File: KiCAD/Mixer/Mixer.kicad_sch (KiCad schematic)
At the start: 20 parts, among them J1 IN_1, J2 IN_2, J3 OUT, J5 Conn_01x03_Socket, J6 Conn_01x03_Socket, Q1 ??, U1 TL072

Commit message: Mixer Schematic
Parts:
- R1, R2, R3, R4, R8: value R -> 100k
- R5: value R -> 1M
- R6: value R -> 220R
- R7: value R -> ??R
- RV1, RV2: value R_Pot -> 100k
- RV3: value NOISE -> 100k NOISE
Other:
- note added: "MYSTERY VERTICAL RESISTOR"
- moved on the sheet: J5, J6

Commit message: Mixer Footprint Association
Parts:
- C1, C2: footprint (none) -> HackSynth:C_Disc_D5.0mm_W2.5mm_P5.00mm
- J1, J2, J3: footprint (none) -> HackSynth:Jack_3.5mm
- R1, R2, R3, R4, R5, R6, R7, R8: footprint (none) -> HackSynth:R_Axial_DIN0207_L6.3mm_D2.5mm_P7.62mm_Horizontal
- RV1, RV2, RV3: footprint (none) -> HackSynth:Potentiometer_Alps_RK09K_Horizontal
- U1: footprint (none) -> HackSynth:DIP-8_W7.62mm_LongPads
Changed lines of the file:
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@@
 			)
 		)
-		(property "Footprint" ""
+		(property "Footprint" "HackSynth:Potentiometer_Alps_RK09K_Horizontal"
 			(at 64.77 104.14 0)
 			(effects
@@
 			)
 		)
-		(property "Footprint" ""
+		(property "Footprint" "HackSynth:Jack_3.5mm"
 			(at 82.55 87.63 0)
 			(effects
@@
 			)
 		)
-		(property "Footprint" ""
+		(property "Footprint" "HackSynth:DIP-8_W7.62mm_LongPads"
 			(at 161.29 118.11 0)
 			(effects
@@
 			)
 		)
-		(property "Footprint" ""
+		(property "Footprint" "HackSynth:R_Axial_DIN0207_L6.3mm_D2.5mm_P7.62mm_Horizontal"
 			(at 123.19 89.408 90)
 			(effects
@@
 			)
 		)
-		(property "Footprint" ""
+		(property "Footprint" "HackSynth:R_Axial_DIN0207_L6.3mm_D2.5mm_P7.62mm_Horizontal"
 			(at 125.222 114.3 90)
 			(effects
@@
 			)
 		)
-		(property "Footprint" ""
+		(property "Footprint" "HackSynth:Potentiometer_Alps_RK09K_Horizontal"
 			(at 127 104.14 0)
 			(effects
@@
 			)
 		)
-		(property "Footprint" ""
+		(property "Footprint" "HackSynth:R_Axial_DIN0207_L6.3mm_D2.5mm_P7.62mm_Horizontal"
 			(at 62.992 114.3 90)
 			(effects
@@
 			)
 		)
-		(property "Footprint" ""
+		(property "Footprint" "HackSynth:R_Axial_DIN0207_L6.3mm_D2.5mm_P7.62mm_Horizontal"
 			(at 146.812 128.27 90)
 			(effects
@@
 			)
 		)
-		(property "Footprint" ""
+		(property "Footprint" "HackSynth:C_Disc_D5.0mm_W2.5mm_P5.00mm"
 			(at 187.6552 121.92 0)
 			(effects
@@
 			)
 		)
-		(property "Footprint" ""
+		(property "Footprint" "HackSynth:Jack_3.5mm"
 			(at 168.91 88.9 0)
 			(effects
@@
 			)
 		)
-		(property "Footprint" ""
+		(property "Footprint" "HackSynth:DIP-8_W7.62mm_LongPads"
 			(at 123.19 66.04 0)
 			(effects
@@
 			)
 		)
-		(property "Footprint" ""
+		(property "Footprint" "HackSynth:R_Axial_DIN0207_L6.3mm_D2.5mm_P7.62mm_Horizontal"
 			(at 87.122 114.3 90)
 			(effects
@@
 			)
 		)
-		(property "Footprint" ""
+		(property "Footprint" "HackSynth:DIP-8_W7.62mm_LongPads"
 			(at 161.29 118.11 0)
 			(effects
@@
 			)
 		)
-		(property "Footprint" ""
+		(property "Footprint" "HackSynth:R_Axial_DIN0207_L6.3mm_D2.5mm_P7.62mm_Horizontal"
 			(at 131.572 43.18 90)
 			(effects
@@
 			)
 		)
-		(property "Footprint" ""
+		(property "Footprint" "HackSynth:R_Axial_DIN0207_L6.3mm_D2.5mm_P7.62mm_Horizontal"
 			(at 105.918 78.74 90)
 			(effects
@@
 			)
 		)
-		(property "Footprint" ""
+		(property "Footprint" "HackSynth:Potentiometer_Alps_RK09K_Horizontal"
 			(at 88.9 104.14 0)
 			(effects
@@
 			)
 		)
-		(property "Footprint" ""
+		(property "Footprint" "HackSynth:C_Disc_D5.0mm_W2.5mm_P5.00mm"
 			(at 119.38 49.8348 0)
 			(effects
@@
 			)
 		)
-		(property "Footprint" ""
+		(property "Footprint" "HackSynth:Jack_3.5mm"
 			(at 58.42 87.63 0)
 			(effects
@@
 			)
 		)
-		(property "Footprint" ""
+		(property "Footprint" "HackSynth:R_Axial_DIN0207_L6.3mm_D2.5mm_P7.62mm_Horizontal"
 			(at 114.808 78.74 90)
 			(effects

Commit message: Mixer Schematic
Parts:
- removed Q1: ??, Package_TO_SOT_THT:TO-92_Inline, symbol Transistor_BJT:2N3905
- added Q2: 2N3904 ?, Package_TO_SOT_THT:TO-92_Inline, symbol Transistor_BJT:2N3904
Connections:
- net GND: now also Q2.2 (B)
- net at C2.2, R8.1: now also Q2.1 (E)
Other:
- note added: "BC547 Fits?"
- note added: "I found a couple of examples of a 2N3904 used as a noise source with pin 3 disconnected. The schematic arrangement doesn't match the photo."
- note added: "https://www.eddybergman.com/2020/05/synthesizer-build-part-31-noise-module.html"
- moved on the sheet: J6

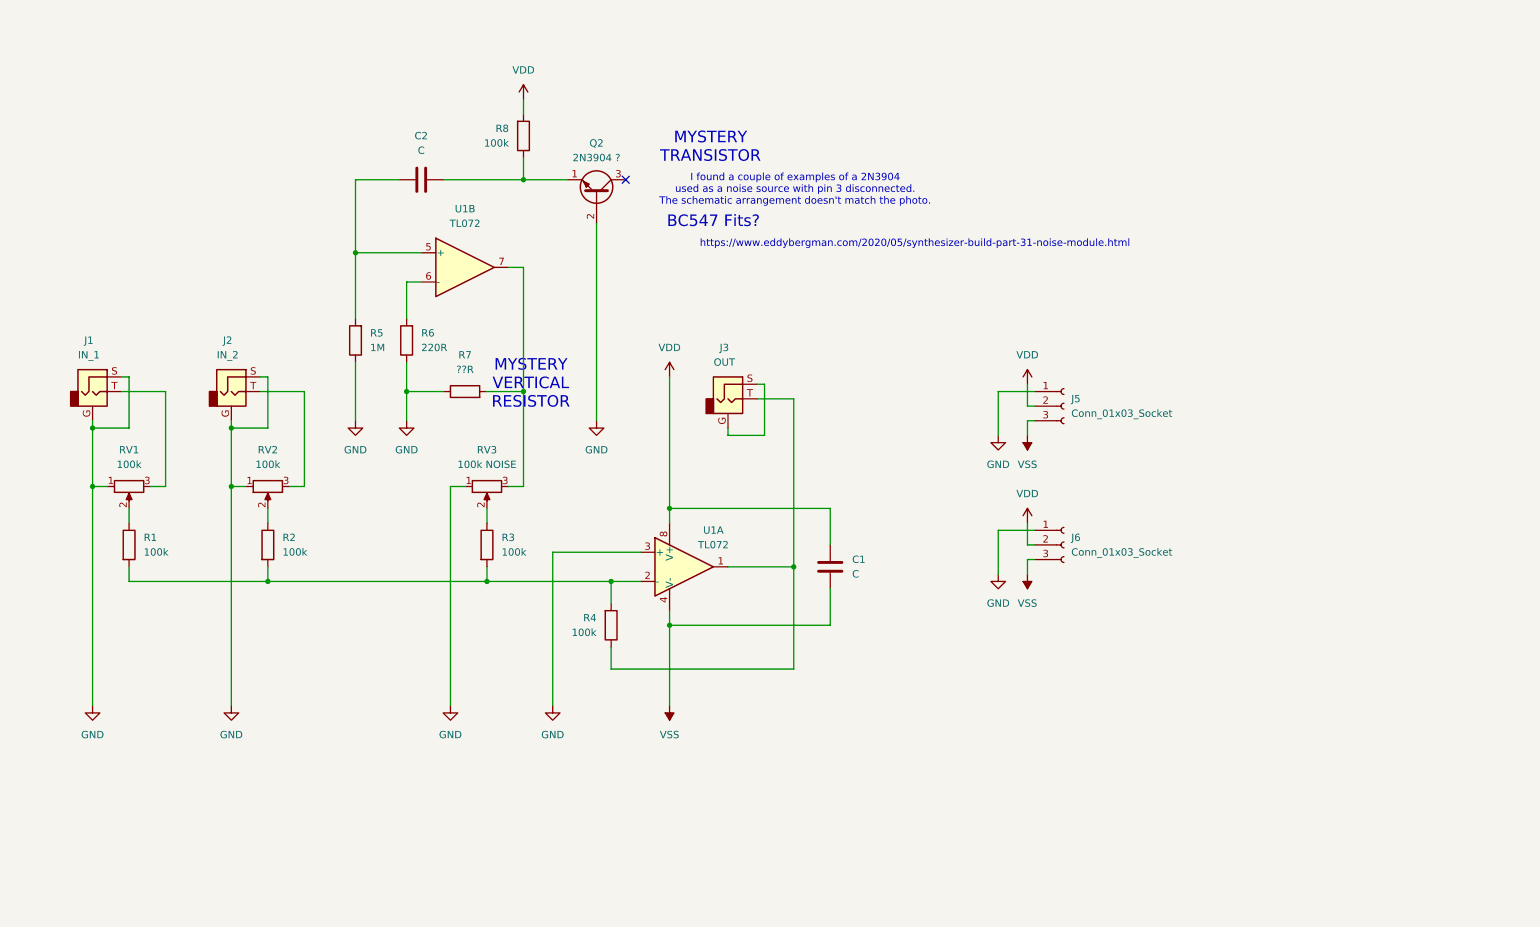
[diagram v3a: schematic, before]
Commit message: Mixer PCB
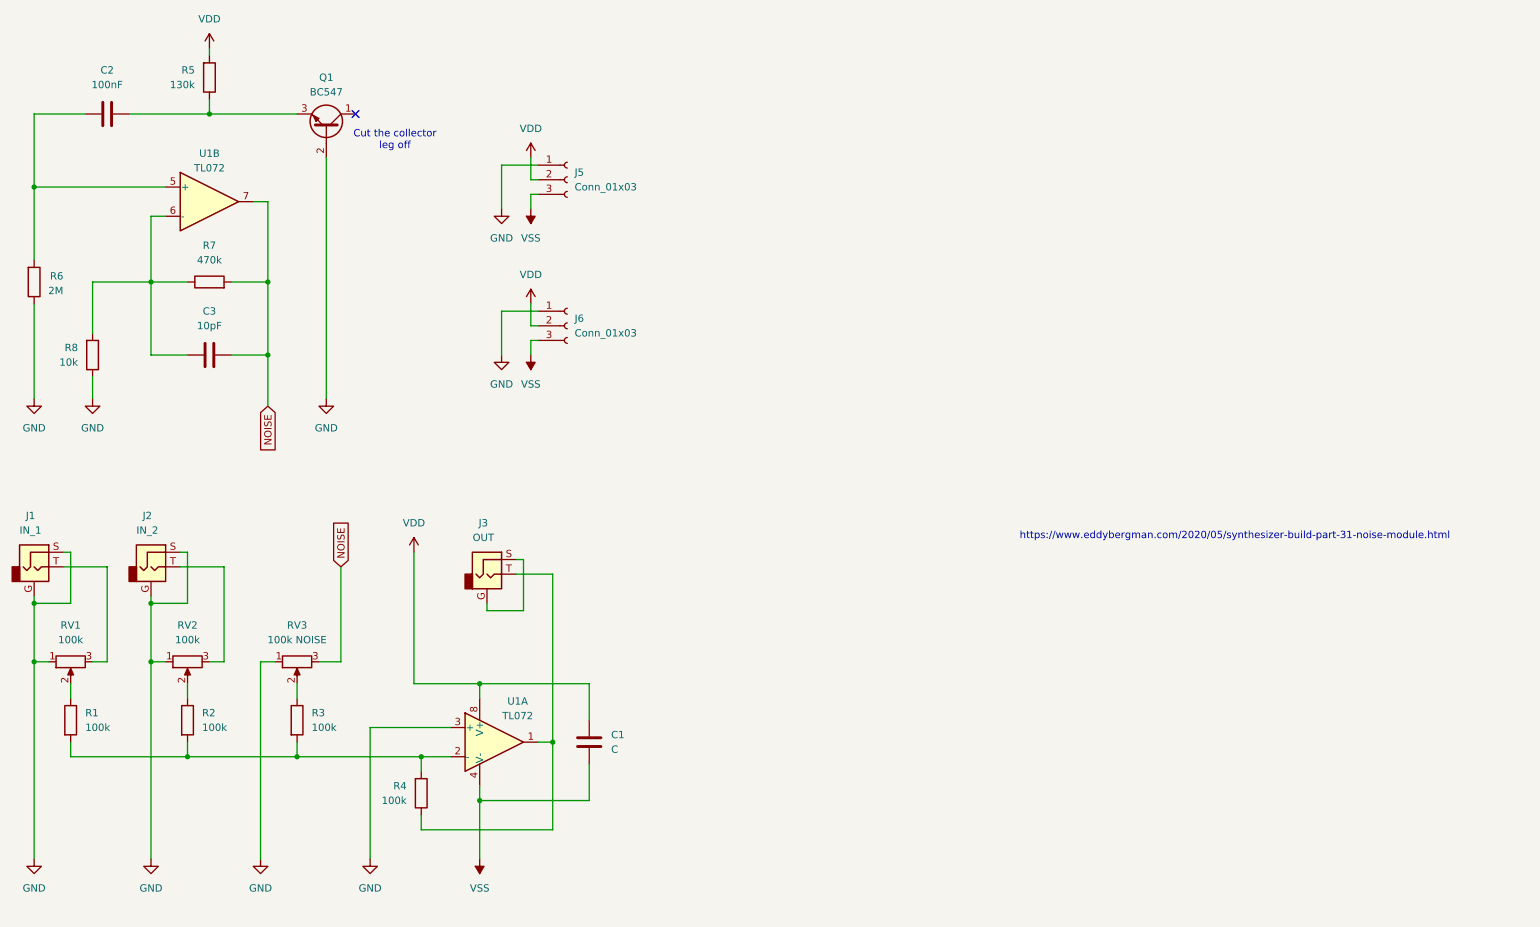
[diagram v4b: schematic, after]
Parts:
- removed Q2: 2N3904 ?, Package_TO_SOT_THT:TO-92_Inline, symbol Transistor_BJT:2N3904
- added C3: 10pF, HackSynth:C_Disc_D5.0mm_W2.5mm_P5.00mm, symbol Device:C
- added Q1: BC547, HackSynth:TO-92_Inline - BC547 - 2-Pin Handsolder, symbol Transistor_BJT:BC547
- C2: value C -> 100nF
- J5, J6: value Conn_01x03_Socket -> Conn_01x03
- R5: value 1M -> 130k
- R6: value 220R -> 2M
- R7: value ??R -> 470k
- R8: value 100k -> 10k
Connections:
- net GND: now also R8.1, Q1.2 (B); no longer R5.1, R7.1
- net VDD: now also R5.2; no longer R8.2
- net NOISE: now reaches R7.2, RV3.3, U1.7
- net NOISE: now also C3.2
- net at C2.2: now also R5.1, Q1.3 (E); no longer R8.1
- net at C2.1, U1.5 (+): now also R6.2; no longer R5.2
- net at U1.6 (-): now also R7.1, R8.2, C3.1; no longer R6.2
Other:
- note added: "Cut the collector leg off"
- note removed: "BC547 Fits?"
- note removed: "I found a couple of examples of a 2N3904 used as a noise source with pin 3 disconnected. The schematic arrangement doesn't match the photo."
- note removed: "MYSTERY TRANSISTOR"
- note removed: "MYSTERY VERTICAL RESISTOR"
- title: (none) -> Mixer + Noise Module
- moved on the sheet: C1, J1, J2, J3, J5, J6, R1, R2, R3, R4, RV1, RV2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

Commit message: Mixer PCB - Gerbers
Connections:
- net GND: now also J3.G, J3.S
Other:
- moved on the sheet: J3
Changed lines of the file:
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@@
 	)
 	(junction
+		(at 125.73 125.73)
+		(diameter 0)
+		(color 0 0 0 0)
+	)
+	(junction
 		(at 68.58 68.58)
 		(diameter 0)
@@
 	(wire
 		(pts
-			(xy 132.08 116.84) (xy 133.35 116.84)
+			(xy 125.73 125.73) (xy 125.73 128.27)
+		)
+		(stroke
+			(width 0)
+			(type default)
+		)
+	)
+	(wire
+		(pts
+			(xy 130.81 116.84) (xy 132.08 116.84)
 		)
 		(stroke
@@
 	(wire
 		(pts
-			(xy 127 125.73) (xy 127 124.46)
+			(xy 125.73 125.73) (xy 125.73 124.46)
 		)
 		(stroke
@@
 	(wire
 		(pts
-			(xy 133.35 116.84) (xy 133.35 125.73)
+			(xy 132.08 116.84) (xy 132.08 125.73)
 		)
 		(stroke
@@
 	(wire
 		(pts
-			(xy 132.08 119.38) (xy 138.43 119.38)
+			(xy 130.81 119.38) (xy 138.43 119.38)
 		)
 		(stroke
@@
 	(wire
 		(pts
-			(xy 127 125.73) (xy 133.35 125.73)
+			(xy 125.73 125.73) (xy 132.08 125.73)
 		)
 		(stroke
@@
 			"ACsALwBCAG4AWgB4AFEAeAAwAFEAaABvAFUANgA5AE8ASQBmAHcASwAwAE0AYwBMAFQAOQAvAFkA"
 			"MABhAC8AMAByAEkAdwBGAGIAdQBIAGMAMABMAEUATQBVADQAagBsAGkARQByAEEAOABSAHoAeABt"
-			"AEsAVgBvAFAAZwBKAEkAMwBlAGMAeAAyAG4AWABhAGUAbwBWAHkAUQBFAFIARQ=="
+			"AEsAVgBvAFAAZwBKAEkAMwBlAGMAeAAyAG4AWABhAGUAbwBWAHkAUQBFAFIARQ4AAAAAAABlp58J"
+			"AAAAAC6EMQUAAAAAKQ4AAAAAAAAUPaAJAAAAAIO3LwUAAAAAKQ4AAAAAAAB5WaMJAAAAAEi6MAUA"
+			"AAAAKg4AAAAAAADKw6IJAAAAAPOGMgUAAAAAKg4AAAAAAADUNKMJAAAAAPOvMAUAAAAAKg4AAAAA"
+			"AADXWaMJAAAAANW4MAUAAAAAKw4AAAAAAADN6KIJAAAAANWPMgUAAAAAKw4AAAAAAACTNKMJAAAA"
+			"AGyxMAUAAAAAKw4AAAAAAACkb6YJAAAAAGs0MQUAAAAALA4AAAAAAADeI6YJAAAAANQSMwUAAAAA"
+			"LA4AAAAAAADYSaYJAAAAAPIvMQUAAAAALA4AAAAAAADKb6YJAAAAAO4yMQUAAAAALQ4AAAAAAADQ"
+			"SaYJAAAAANAVMwUAAAAALQ4AAAAAAADQSaYJAAAAAHAxMQUAAAAALQ4AAAAAAAAwj6kJAAAAAHAx"
+			"MQUAAAAALg4AAAAAAAAwj6kJAAAAANAVMwUAAAAALg4AAAAAAAA2aakJAAAAAO4yMQUAAAAALg4A"
+			"AAAAAAAoj6kJAAAAAPIvMQUAAAAALw4AAAAAAAAitakJAAAAANQSMwUAAAAALw4AAAAAAABcaakJ"
+			"AAAAAGs0MQUAAAAALw4AAAAAAABtpKwJAAAAAGyxMAUAAAAAMA4AAAAAAAAz8KwJAAAAANWPMgUA"
+			"AAAAMA4AAAAAAAApf6wJAAAAANW4MAUAAAAAMA4AAAAAAAAspKwJAAAAAPOvMAUAAAAAMQ4AAAAA"
+			"AAA2Fa0JAAAAAPOGMgUAAAAAMQ4AAAAAAACHf6wJAAAAAEi6MAUAAAAAMQ4AAAAAAADsm68JAAAA"
+			"AIO3LwUAAAAAMg4AAAAAAACbMbAJAAAAAC6EMQUAAAAAMg4AAAAAAABGeK8JAAAAAKrELwUAAAAA"
+			"Mg4AAAAAAABwm68JAAAAABq2LwUAAAAAMw4AAAAAAADFVLAJAAAAAJ51MQUAAAAAMw4AAAAAAADe"
+			"eK8JAAAAAAnGLwUAAAAAMw4AAAAAAAD6YrIJAAAAAOBJLgUAAAAANA4AAAAAAADhPrMJAAAAAHX5"
+			"LwUAAAAANA4AAAAAAADJQbIJAAAAAHdcLgUAAAAANA4AAAAAAAA+YrIJAAAAAJNILgUAAAAANQ4A"
+			"AAAAAABWX7MJAAAAAJHlLwUAAAAANQ4AAAAAAACfQrIJAAAAALRdLgUAAAAANQ4AAAAAAADItLMJ"
+			"AAAAAMJQLQUAAAAANg4AAAAAAAB/0bQJAAAAAJ/YLgUAAAAANg4AAAAAAACd7rIJAAAAAJ6yLgUA"
+			"AAAANg4AAAAAAACnEbMJAAAAAGb1LAUAAAAANw4AAAAAAACJ9LQJAAAAAGcbLQ=="
 		)
 	)
@@
 	(symbol
 		(lib_id "HackSynth:AudioJack2_Ground")
-		(at 127 119.38 0)
+		(at 125.73 119.38 0)
 		(unit 1)
 		(exclude_from_sim no)
@@
 		(fields_autoplaced yes)
 		(property "Reference" "J3"
-			(at 126.365 110.49 0)
+			(at 125.095 110.49 0)
 			(effects
 				(font
@@
 		)
 		(property "Value" "OUT"
-			(at 126.365 113.03 0)
+			(at 125.095 113.03 0)
 			(effects
 				(font
@@
 		)
 		(property "Footprint" "HackSynth:Jack_3.5mm"
-			(at 127 119.38 0)
+			(at 125.73 119.38 0)
 			(effects
 				(font
@@
 		)
 		(property "Datasheet" "~"
-			(at 127 119.38 0)
+			(at 125.73 119.38 0)
 			(effects
 				(font
@@
 		)
 		(property "Description" "Audio Jack, 2 Poles (Mono / TS), Grounded Sleeve"
-			(at 127 119.38 0)
+			(at 125.73 119.38 0)
 			(effects
 				(font
@@
 					(unit 1)
 				)
+			)
+		)
+	)
+	(symbol
+		(lib_id "power:GND")
+		(at 125.73 128.27 0)
+		(unit 1)
+		(exclude_from_sim no)
+		(in_bom yes)
+		(on_board yes)
+		(dnp no)
+		(property "Reference" "#PWR04"
+			(at 125.73 134.62 0)
+			(effects
+				(font
+					(size 1.27 1.27)
+				)
+				(hide yes)
+			)
+		)
+		(property "Value" "GND"
+			(at 125.73 133.35 0)
+			(effects
+				(font
+					(size 1.27 1.27)
+				)
+			)
+		)
+		(property "Footprint" ""
+			(at 125.73 128.27 0)
+			(effects
+				(font
+					(size 1.27 1.27)
+				)
+				(hide yes)
+			)
+		)
+		(property "Datasheet" ""
+			(at 125.73 128.27 0)
+			(effects
+				(font
+					(size 1.27 1.27)
+				)
+				(hide yes)
+			)
+		)
+		(property "Description" "Power symbol creates a global label with name \"GND\" , ground"
+			(at 125.73 128.27 0)
+			(effects
+				(font
+					(size 1.27 1.27)
+				)
+				(hide yes)
+			)
+		)
+		(pin "1"
+		)
+		(instances
+			(project "Mixer"
+				(path "/d4613ad6-090f-4725-80fe-a4c191d32f09"
+					(reference "#PWR04")
+					(unit 1)
+				)

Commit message: Backup Cleanup
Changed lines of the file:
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@@
 		(dnp no)
 		(property "Reference" "R4"
-			(at 113.03 156.2099 0)
+			(at 113.03 156.464 0)
 			(effects
 				(font
@@
 		)
 		(property "Value" "100k"
-			(at 113.03 158.7499 0)
+			(at 113.03 158.496 0)
 			(effects
 				(font
@@
 		(on_board yes)
 		(dnp no)
-		(fields_autoplaced yes)
 		(property "Reference" "C3"
-			(at 78.74 73.66 90)
+			(at 78.74 75.184 90)
 			(effects
 				(font
@@
 		)
 		(property "Value" "10pF"
-			(at 78.74 76.2 90)
+			(at 78.74 77.216 90)
 			(effects
 				(font
@@
 		(dnp no)
 		(property "Reference" "R6"
-			(at 53.34 67.564 0)
-			(effects
-				(font
-					(size 1.27 1.27)
-				)
-				(justify right)
+			(at 50.292 67.564 0)
+			(effects
+				(font
+					(size 1.27 1.27)
+				)
+				(justify left)
 			)
 		)
 		(property "Value" "2M"
-			(at 53.34 70.104 0)
-			(effects
-				(font
-					(size 1.27 1.27)
-				)
-				(justify right)
+			(at 50.292 69.596 0)
+			(effects
+				(font
+					(size 1.27 1.27)
+				)
+				(justify left)
 			)
 		)
@@
 		(on_board yes)
 		(dnp no)
-		(fields_autoplaced yes)
 		(property "Reference" "R7"
-			(at 78.74 62.23 90)
+			(at 78.74 66.294 90)
 			(effects
 				(font
@@
 		)
 		(property "Value" "470k"
-			(at 78.74 64.77 90)
+			(at 78.74 68.58 90)
 			(effects
 				(font
@@
 		(dnp no)
 		(property "Reference" "R8"
-			(at 55.88 80.0099 0)
+			(at 56.134 80.264 0)
 			(effects
 				(font
@@
 		)
 		(property "Value" "10k"
-			(at 55.88 82.5499 0)
-			(effects
-				(font
+			(at 56.134 82.2959 0)
+			(effects
+				(font

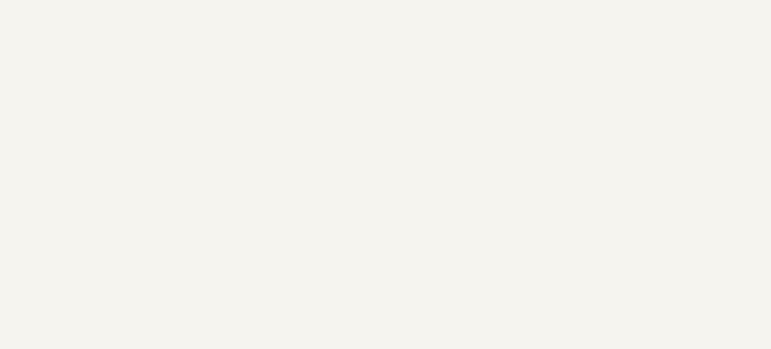
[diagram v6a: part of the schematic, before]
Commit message: Footprint Edits
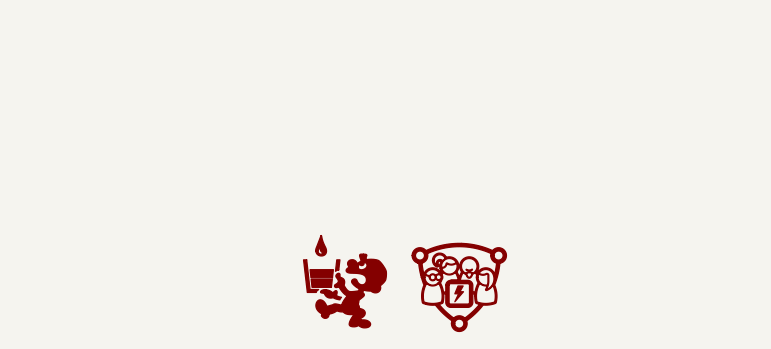
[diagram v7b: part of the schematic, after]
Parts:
- added G1: ~, symbol HackSynth:CCHS_Logo
- added G2: ~, symbol HackSynth:Logo_PancakeLegend
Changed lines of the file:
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@@
+	)
+	(symbol
+		(lib_id "HackSynth:CCHS_Logo")
+		(at 275.59 172.72 0)
+		(unit 1)
+		(exclude_from_sim no)
+		(in_bom yes)
+		(on_board yes)
+		(dnp no)
+		(fields_autoplaced yes)
+		(property "Reference" "G1"
+			(at 275.59 180.34 0)
+			(effects
+				(font
+					(size 1.27 1.27)
+				)
+				(hide yes)
+			)
+		)
+		(property "Value" "~"
+			(at 281.94 173.89 0)
+			(effects
+				(font
+					(size 1.27 1.27)
+				)
+				(justify left)
+			)
+		)
+		(property "Footprint" ""
+			(at 275.59 172.72 0)
+			(effects
+				(font
+					(size 1.27 1.27)
+				)
+				(hide yes)
+			)
+		)
+		(property "Datasheet" ""
+			(at 275.59 172.72 0)
+			(effects
+				(font
+					(size 1.27 1.27)
+				)
+				(hide yes)
+			)
+		)
+		(property "Description" ""
+			(at 275.59 172.72 0)
+			(effects
+				(font
+					(size 1.27 1.27)
+				)
+				(hide yes)
+			)
+		)
+		(instances
+			(project "Mixer"
+				(path "/d4613ad6-090f-4725-80fe-a4c191d32f09"
+					(reference "G1")
+					(unit 1)
+				)
+			)
+		)
 	)
 	(symbol
@@
 				)
 			)
+		)
+	)
+	(symbol
+		(lib_id "HackSynth:Logo_PancakeLegend")
+		(at 262.89 173.355 0)
+		(unit 1)
+		(exclude_from_sim no)
+		(in_bom yes)
+		(on_board yes)
+		(dnp no)
+		(fields_autoplaced yes)
+		(property "Reference" "G2"
+			(at 262.89 180.975 0)
+			(effects
+				(font
+					(size 1.27 1.27)
+				)
+				(hide yes)
+			)
+		)
+		(property "Value" "~"
+			(at 269.24 173.2549 0)
+			(effects
+				(font
+					(size 1.27 1.27)
+				)
+				(justify left)
+			)
+		)
+		(property "Footprint" ""
+			(at 262.89 173.355 0)
+			(effects
+				(font
+					(size 1.27 1.27)
+				)
+				(hide yes)
+			)
+		)
+		(property "Datasheet" ""
+			(at 262.89 173.355 0)
+			(effects
+				(font
+					(size 1.27 1.27)
+				)
+				(hide yes)
+			)
+		)
+		(property "Description" ""
+			(at 262.89 173.355 0)
+			(effects
+				(font
+					(size 1.27 1.27)
+				)
+				(hide yes)
+			)
+		)
+		(instances
+			(project "Mixer"
+				(path "/d4613ad6-090f-4725-80fe-a4c191d32f09"
+					(reference "G2")
+					(unit 1)
+				)
+			)
